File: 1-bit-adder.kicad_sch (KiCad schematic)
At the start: 3 parts, among them U10 74LS32, U2 74HC86, U6 74LS08

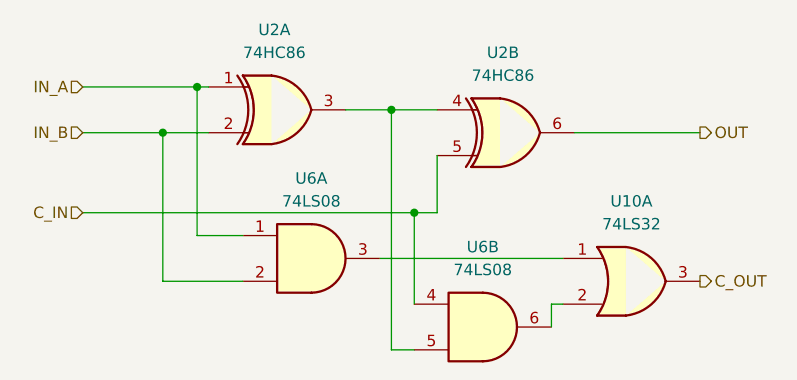
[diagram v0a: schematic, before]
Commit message: feat: working 4-bit adder (normally)
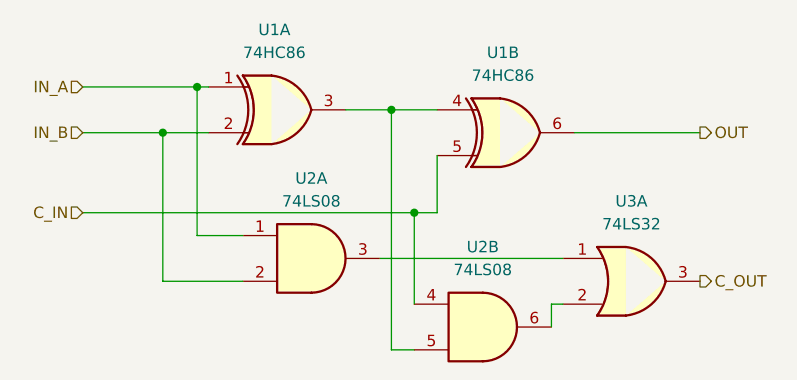
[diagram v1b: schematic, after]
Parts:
- renumbered U2 to U1, U6 to U2, U10 to U3
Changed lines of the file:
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@@
 		(dnp no)
 		(fields_autoplaced yes)
-		(property "Reference" "U2"
+		(property "Reference" "U1"
 			(at 89.8652 68.58 0)
 			(effects
@@
 			(project ""
 				(path "/4987240f-8890-46b8-b8e9-0d60580cb205/10a3732c-bf63-42c8-b0c5-c029ff8b8938"
-					(reference "U2")
+					(reference "U1")
 					(unit 2)
 				)
 				(path "/4987240f-8890-46b8-b8e9-0d60580cb205/2ab78124-47e9-4404-842f-89ef59ad6ac3"
-					(reference "U5")
-					(unit 2)
+					(reference "U4")
+					(unit 4)
 				)
 				(path "/4987240f-8890-46b8-b8e9-0d60580cb205/d1db8f6e-5205-451b-aac4-82dec57d8ab8"
@@
 				)
 				(path "/4987240f-8890-46b8-b8e9-0d60580cb205/dde0e48b-d316-4fbd-8778-cd8a135129ba"
-					(reference "U3")
-					(unit 2)
+					(reference "U1")
+					(unit 4)
 				)
 			)
@@
 		(dnp no)
 		(fields_autoplaced yes)
-		(property "Reference" "U2"
+		(property "Reference" "U1"
 			(at 64.4652 66.04 0)
 			(effects
@@
 			(project ""
 				(path "/4987240f-8890-46b8-b8e9-0d60580cb205/10a3732c-bf63-42c8-b0c5-c029ff8b8938"
-					(reference "U2")
+					(reference "U1")
 					(unit 1)
 				)
 				(path "/4987240f-8890-46b8-b8e9-0d60580cb205/2ab78124-47e9-4404-842f-89ef59ad6ac3"
-					(reference "U5")
-					(unit 1)
+					(reference "U4")
+					(unit 3)
 				)
 				(path "/4987240f-8890-46b8-b8e9-0d60580cb205/d1db8f6e-5205-451b-aac4-82dec57d8ab8"
@@
 				)
 				(path "/4987240f-8890-46b8-b8e9-0d60580cb205/dde0e48b-d316-4fbd-8778-cd8a135129ba"
-					(reference "U3")
-					(unit 1)
+					(reference "U1")
+					(unit 3)
 				)
 			)
@@
 		(dnp no)
 		(fields_autoplaced yes)
-		(property "Reference" "U10"
+		(property "Reference" "U3"
 			(at 104.14 85.09 0)
 			(effects
@@
 			(project ""
 				(path "/4987240f-8890-46b8-b8e9-0d60580cb205/10a3732c-bf63-42c8-b0c5-c029ff8b8938"
-					(reference "U10")
+					(reference "U3")
 					(unit 1)
 				)
 				(path "/4987240f-8890-46b8-b8e9-0d60580cb205/2ab78124-47e9-4404-842f-89ef59ad6ac3"
-					(reference "U13")
-					(unit 1)
+					(reference "U3")
+					(unit 4)
 				)
 				(path "/4987240f-8890-46b8-b8e9-0d60580cb205/d1db8f6e-5205-451b-aac4-82dec57d8ab8"
-					(reference "U12")
-					(unit 1)
+					(reference "U3")
+					(unit 3)
 				)
 				(path "/4987240f-8890-46b8-b8e9-0d60580cb205/dde0e48b-d316-4fbd-8778-cd8a135129ba"
-					(reference "U11")
-					(unit 1)
+					(reference "U3")
+					(unit 2)
 				)
 			)
@@
 		(dnp no)
 		(fields_autoplaced yes)
-		(property "Reference" "U6"
+		(property "Reference" "U2"
 			(at 68.5717 82.55 0)
 			(effects
@@
 			(project ""
 				(path "/4987240f-8890-46b8-b8e9-0d60580cb205/10a3732c-bf63-42c8-b0c5-c029ff8b8938"
-					(reference "U6")
+					(reference "U2")
 					(unit 1)
 				)
 				(path "/4987240f-8890-46b8-b8e9-0d60580cb205/2ab78124-47e9-4404-842f-89ef59ad6ac3"
-					(reference "U9")
+					(reference "U5")
+					(unit 3)
+				)
+				(path "/4987240f-8890-46b8-b8e9-0d60580cb205/d1db8f6e-5205-451b-aac4-82dec57d8ab8"
+					(reference "U5")
 					(unit 1)
 				)
-				(path "/4987240f-8890-46b8-b8e9-0d60580cb205/d1db8f6e-5205-451b-aac4-82dec57d8ab8"
-					(reference "U8")
-					(unit 1)
-				)
 				(path "/4987240f-8890-46b8-b8e9-0d60580cb205/dde0e48b-d316-4fbd-8778-cd8a135129ba"
-					(reference "U7")
-					(unit 1)
+					(reference "U2")
+					(unit 3)
 				)
 			)
@@
 		(dnp no)
 		(fields_autoplaced yes)
-		(property "Reference" "U6"
+		(property "Reference" "U2"
 			(at 87.6217 90.17 0)
 			(effects
@@
 			(project ""
 				(path "/4987240f-8890-46b8-b8e9-0d60580cb205/10a3732c-bf63-42c8-b0c5-c029ff8b8938"
-					(reference "U6")
+					(reference "U2")
 					(unit 2)
 				)
 				(path "/4987240f-8890-46b8-b8e9-0d60580cb205/2ab78124-47e9-4404-842f-89ef59ad6ac3"
-					(reference "U9")
+					(reference "U5")
+					(unit 4)
+				)
+				(path "/4987240f-8890-46b8-b8e9-0d60580cb205/d1db8f6e-5205-451b-aac4-82dec57d8ab8"
+					(reference "U5")
 					(unit 2)
 				)
-				(path "/4987240f-8890-46b8-b8e9-0d60580cb205/d1db8f6e-5205-451b-aac4-82dec57d8ab8"
-					(reference "U8")
-					(unit 2)
-				)
 				(path "/4987240f-8890-46b8-b8e9-0d60580cb205/dde0e48b-d316-4fbd-8778-cd8a135129ba"
-					(reference "U7")
-					(unit 2)
-				)
-			)
+					(reference "U2")
+					(unit 4)
+				)
+			)

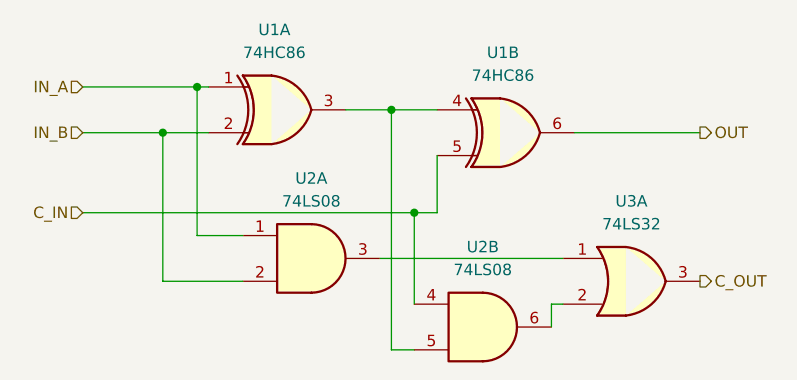
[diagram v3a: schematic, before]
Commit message: feat: footprints on gates
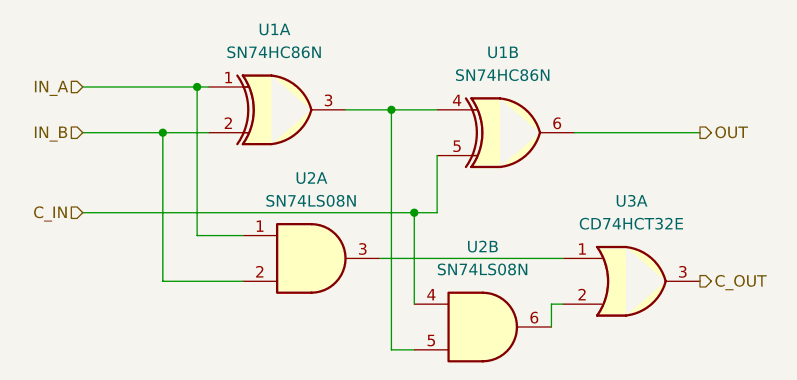
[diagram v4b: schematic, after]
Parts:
- U1: value 74HC86 -> SN74HC86N; footprint (none) -> Package_DIP:DIP-14_W7.62mm_LongPads
- U2: value 74LS08 -> SN74LS08N; footprint (none) -> Package_DIP:DIP-14_W7.62mm_LongPads
- U3: value 74LS32 -> CD74HCT32E; footprint (none) -> Package_DIP:DIP-14_W7.62mm_LongPads
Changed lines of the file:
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@@
 			)
 		)
-		(property "Value" "74HC86"
+		(property "Value" "SN74HC86N"
 			(at 89.8652 71.12 0)
 			(show_name no)
@@
 			)
 		)
-		(property "Footprint" ""
+		(property "Footprint" "Package_DIP:DIP-14_W7.62mm_LongPads"
 			(at 90.17 77.47 0)
 			(hide yes)
@@
 			)
 		)
-		(property "Value" "74HC86"
+		(property "Value" "SN74HC86N"
 			(at 64.4652 68.58 0)
 			(show_name no)
@@
 			)
 		)
-		(property "Footprint" ""
+		(property "Footprint" "Package_DIP:DIP-14_W7.62mm_LongPads"
 			(at 64.77 74.93 0)
 			(hide yes)
@@
 			)
 		)
-		(property "Value" "74LS32"
+		(property "Value" "CD74HCT32E"
 			(at 104.14 87.63 0)
 			(show_name no)
@@
 			)
 		)
-		(property "Footprint" ""
+		(property "Footprint" "Package_DIP:DIP-14_W7.62mm_LongPads"
 			(at 104.14 93.98 0)
 			(hide yes)
@@
 			)
 		)
-		(property "Datasheet" "http://www.ti.com/lit/gpn/sn74LS32"
+		(property "Datasheet" "https://www.ti.com/lit/ds/symlink/cd54hct32.pdf"
 			(at 104.14 93.98 0)
 			(hide yes)
@@
 			)
 		)
-		(property "Value" "74LS08"
+		(property "Value" "SN74LS08N"
 			(at 68.5717 85.09 0)
 			(show_name no)
@@
 			)
 		)
-		(property "Footprint" ""
+		(property "Footprint" "Package_DIP:DIP-14_W7.62mm_LongPads"
 			(at 68.58 91.44 0)
 			(hide yes)
@@
 			)
 		)
-		(property "Datasheet" "http://www.ti.com/lit/gpn/sn74LS08"
+		(property "Datasheet" "https://www.ti.com/lit/ds/symlink/sn74hc86.pdf"
 			(at 68.58 91.44 0)
 			(hide yes)
@@
 			)
 		)
-		(property "Value" "74LS08"
+		(property "Value" "SN74LS08N"
 			(at 87.6217 92.71 0)
 			(show_name no)
@@
 			)
 		)
-		(property "Footprint" ""
+		(property "Footprint" "Package_DIP:DIP-14_W7.62mm_LongPads"
 			(at 87.63 99.06 0)
 			(hide yes)
@@
 			)
 		)
-		(property "Datasheet" "http://www.ti.com/lit/gpn/sn74LS08"
+		(property "Datasheet" "https://www.ti.com/lit/ds/symlink/sn74hc86.pdf"
 			(at 87.63 99.06 0)
 			(hide yes)

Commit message: fix: merge
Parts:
- renumbered U2 to U0, U3 to U5
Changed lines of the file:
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@@
 				)
 				(path "/4987240f-8890-46b8-b8e9-0d60580cb205/2ab78124-47e9-4404-842f-89ef59ad6ac3"
-					(reference "U4")
+					(reference "U2")
 					(unit 4)
 				)
 				(path "/4987240f-8890-46b8-b8e9-0d60580cb205/d1db8f6e-5205-451b-aac4-82dec57d8ab8"
-					(reference "U4")
+					(reference "U2")
 					(unit 2)
 				)
@@
 				)
 				(path "/4987240f-8890-46b8-b8e9-0d60580cb205/2ab78124-47e9-4404-842f-89ef59ad6ac3"
-					(reference "U4")
+					(reference "U2")
 					(unit 3)
 				)
 				(path "/4987240f-8890-46b8-b8e9-0d60580cb205/d1db8f6e-5205-451b-aac4-82dec57d8ab8"
-					(reference "U4")
+					(reference "U2")
 					(unit 1)
 				)
@@
 		(dnp no)
 		(fields_autoplaced yes)
-		(property "Reference" "U3"
+		(property "Reference" "U5"
 			(at 104.14 85.09 0)
 			(show_name no)
@@
 			(project "alu"
 				(path "/4987240f-8890-46b8-b8e9-0d60580cb205/10a3732c-bf63-42c8-b0c5-c029ff8b8938"
-					(reference "U3")
+					(reference "U5")
 					(unit 1)
 				)
 				(path "/4987240f-8890-46b8-b8e9-0d60580cb205/2ab78124-47e9-4404-842f-89ef59ad6ac3"
-					(reference "U3")
+					(reference "U5")
 					(unit 4)
 				)
 				(path "/4987240f-8890-46b8-b8e9-0d60580cb205/d1db8f6e-5205-451b-aac4-82dec57d8ab8"
-					(reference "U3")
+					(reference "U5")
 					(unit 3)
 				)
 				(path "/4987240f-8890-46b8-b8e9-0d60580cb205/dde0e48b-d316-4fbd-8778-cd8a135129ba"
-					(reference "U3")
+					(reference "U5")
 					(unit 2)
 				)
@@
 		(dnp no)
 		(fields_autoplaced yes)
-		(property "Reference" "U2"
+		(property "Reference" "U0"
 			(at 68.5717 82.55 0)
 			(show_name no)
@@
 			(project "alu"
 				(path "/4987240f-8890-46b8-b8e9-0d60580cb205/10a3732c-bf63-42c8-b0c5-c029ff8b8938"
-					(reference "U2")
+					(reference "U0")
 					(unit 1)
 				)
 				(path "/4987240f-8890-46b8-b8e9-0d60580cb205/2ab78124-47e9-4404-842f-89ef59ad6ac3"
-					(reference "U5")
+					(reference "U3")
 					(unit 3)
 				)
 				(path "/4987240f-8890-46b8-b8e9-0d60580cb205/d1db8f6e-5205-451b-aac4-82dec57d8ab8"
-					(reference "U5")
+					(reference "U3")
 					(unit 1)
 				)
 				(path "/4987240f-8890-46b8-b8e9-0d60580cb205/dde0e48b-d316-4fbd-8778-cd8a135129ba"
-					(reference "U2")
+					(reference "U0")
 					(unit 3)
 				)
@@
 		(dnp no)
 		(fields_autoplaced yes)
-		(property "Reference" "U2"
+		(property "Reference" "U0"
 			(at 87.6217 90.17 0)
 			(show_name no)
@@
 			(project "alu"
 				(path "/4987240f-8890-46b8-b8e9-0d60580cb205/10a3732c-bf63-42c8-b0c5-c029ff8b8938"
-					(reference "U2")
+					(reference "U0")
 					(unit 2)
 				)
 				(path "/4987240f-8890-46b8-b8e9-0d60580cb205/2ab78124-47e9-4404-842f-89ef59ad6ac3"
-					(reference "U5")
+					(reference "U3")
 					(unit 4)
 				)
 				(path "/4987240f-8890-46b8-b8e9-0d60580cb205/d1db8f6e-5205-451b-aac4-82dec57d8ab8"
-					(reference "U5")
+					(reference "U3")
 					(unit 2)
 				)
 				(path "/4987240f-8890-46b8-b8e9-0d60580cb205/dde0e48b-d316-4fbd-8778-cd8a135129ba"
-					(reference "U2")
+					(reference "U0")
 					(unit 4)
 				)
